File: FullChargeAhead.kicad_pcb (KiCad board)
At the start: 2 copper layers, 18 parts, among them P101 USB_OTG, P102 CONN_01X02, U101 MCP73834

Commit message: starting rev 2
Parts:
- removed D103: NOPOP, LEDs:LED_0805
- removed R106: NOPOP, Resistors_SMD:R_0805_HandSoldering
- added P103: JST_2PIN, FullChargeAhead:JST_Type_PH_Side_Entry_1x02_Pitch2.00mm, F.Cu at (164.2, 91.2)
- added R110: 10K, Resistors_SMD:R_0805_HandSoldering, F.Cu at (166.0, 102.7)
- P101: footprint Connect:USB_Micro-B_10103594-0001LF -> FullChargeAhead:USB_Micro-B_10103594-0001LF
- P102: footprint Connect:PINHEAD1-2 -> Pin_Headers:Pin_Header_Straight_1x02
- R107: value 38.3R -> 1K
- R108: value 0R -> 38.3R
- R109: value 10K -> 0R
- moved R103 82.8 mm to (129.8, 96.6), turned to 90 degrees
- moved D102 80.2 mm to (140.7, 103.5), turned to 180 degrees
- moved R102 75.4 mm to (132.5, 96.6), turned to 90 degrees
- moved D101 73.4 mm to (140.7, 101.0), turned to 180 degrees
- moved R101 68.6 mm to (135.1, 96.7), turned to 90 degrees
- moved P101 62.5 mm to (132.5, 89.2), turned to 180 degrees
- moved R105 62.3 mm to (145.9, 103.5)
- moved C101 60.8 mm to (141.9, 95.5)
- moved R104 59.2 mm to (145.9, 101.0)
- moved R109 57.0 mm to (160.4, 102.9), turned to 180 degrees
- moved R108 55.2 mm to (154.2, 105.8), turned to 180 degrees
- moved R107 51.2 mm to (160.0, 106.9)
- moved C102 44.8 mm to (164.1, 95.6), turned to 180 degrees
- moved U101 43.7 mm to (153.7, 102.2)
- moved P102 32.0 mm to (164.9, 107.6), turned to 90 degrees
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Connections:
- P102 pad 1: /Vbat -> Net-(P102-Pad1)
- R107 pad 2: GND -> Net-(P102-Pad1)
- R108 pad 2: Net-(R108-Pad2) -> GND
- R109 pad 1: GND -> Net-(R109-Pad1)
- R109 pad 2: Net-(R108-Pad1) -> Net-(R109-Pad2)
- TH101 pad 1: Net-(R108-Pad1) -> Net-(R109-Pad1)
- U101 pad 6: Net-(R107-Pad1) -> Net-(R108-Pad1)
- U101 pad 7: Net-(R106-Pad2) -> Net-(R107-Pad1)
- U101 pad 8: Net-(R108-Pad2) -> Net-(R109-Pad2)

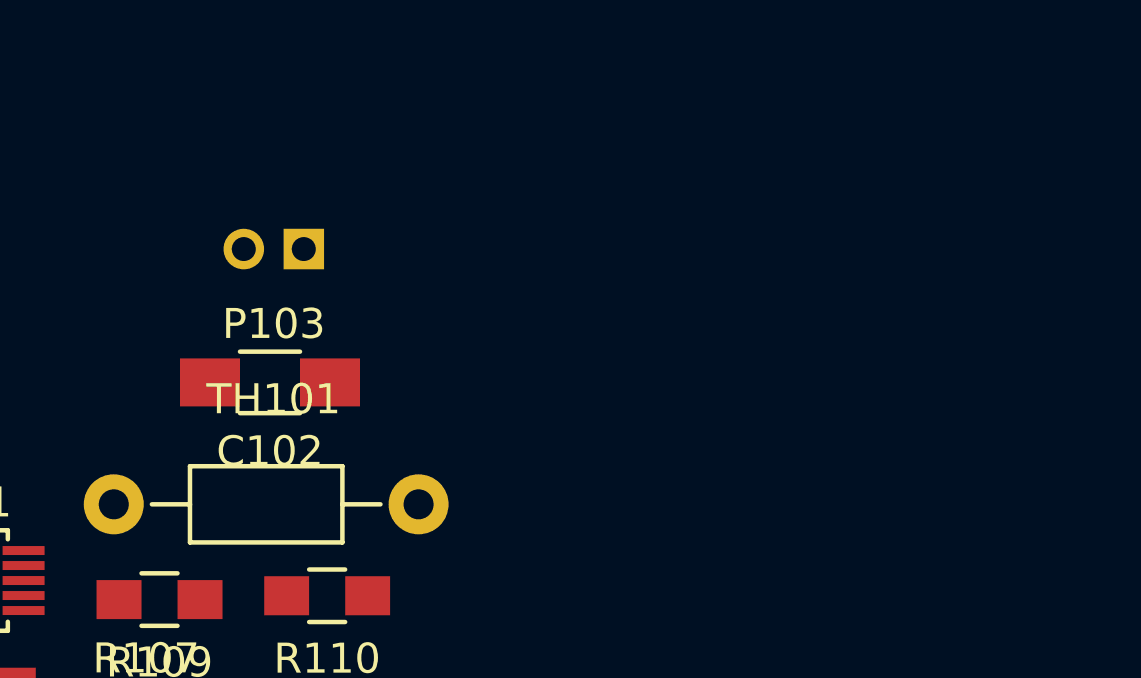
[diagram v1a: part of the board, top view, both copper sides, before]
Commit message: added Vbat connectors for current monitoring
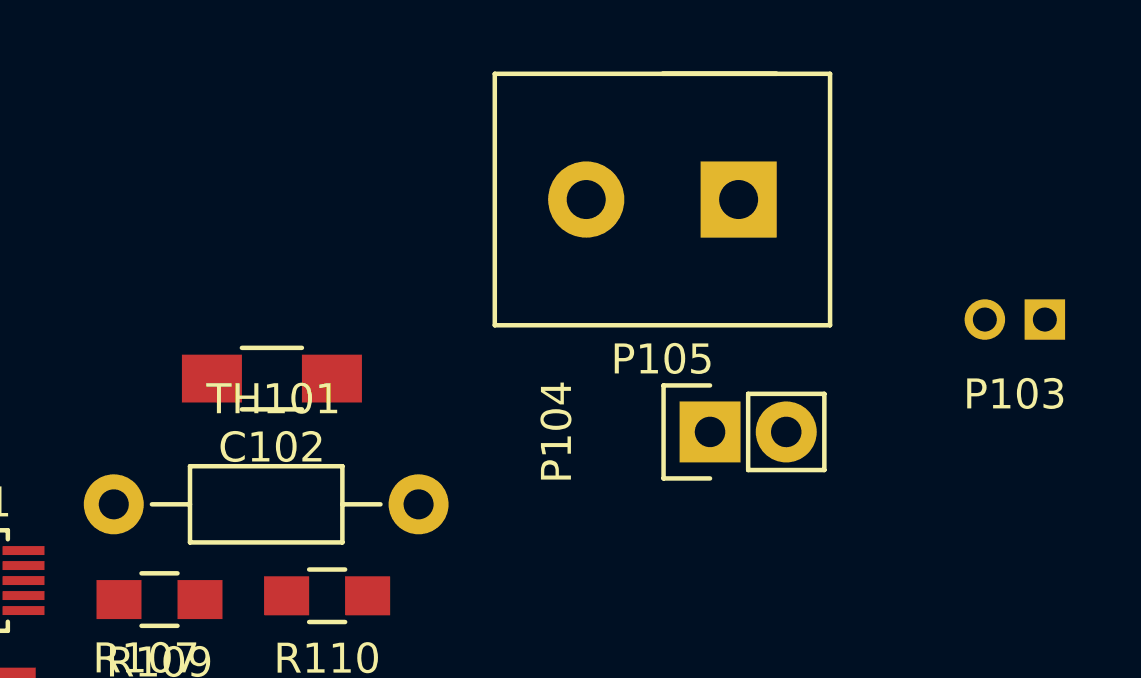
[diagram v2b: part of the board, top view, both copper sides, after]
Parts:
- added P104: CONN_01X02, Pin_Headers:Pin_Header_Straight_1x02, F.Cu at (178.8, 97.3)
- added P105: CONN_01X02, FullChargeAhead:Terminal_Block_200_mil, F.Cu at (177.2, 89.5)
- moved P103 24.8 mm to (188.9, 93.5)
- moved C102 0.14 mm to (164.1, 95.5)
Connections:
- P103 pad 1: /Vbat -> /Vbat2
- R110 pad 2: Net-(R109-Pad1) -> Net-(R110-Pad2)
- U101 pad 8: Net-(R109-Pad2) -> Net-(R110-Pad2)
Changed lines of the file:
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@@
 (kicad_pcb (version 4) (host pcbnew 4.0.2-stable)
   (general
-    (links 38)
-    (no_connects 38)
+    (links 40)
+    (no_connects 40)
     (area 0 0 0 0)
     (thickness 1.6)
@@
     (tracks 0)
     (zones 0)
-    (modules 18)
-    (nets 16)
+    (modules 20)
+    (nets 18)
   )
   (page A4)
@@
   (net 14 "Net-(R109-Pad2)")
   (net 15 "Net-(R107-Pad1)")
+  (net 16 /Vbat2)
+  (net 17 "Net-(R110-Pad2)")
   (net_class Default "This is the default net class."
     (clearance 0.2)
@@
     (uvia_drill 0.1)
     (add_net /Vbat)
+    (add_net /Vbat2)
     (add_net /Vdd)
     (add_net GND)
@@
     (add_net "Net-(R109-Pad1)")
     (add_net "Net-(R109-Pad2)")
+    (add_net "Net-(R110-Pad2)")
   )
   (module LEDs:LED_0805 (layer F.Cu)
@@
   )
   (module Capacitors_SMD:C_1206_HandSoldering (layer F.Cu)
-    (at 164.084 95.631 180)
+    (at 164.1475 95.504 180)
     (descr "Capacitor SMD 1206, hand soldering")
     (tags "capacitor 1206")
@@
       (net 15 "Net-(R107-Pad1)"))
     (pad 8 smd rect (at 2.2 0) (size 1.4 0.3) (layers F.Cu F.Paste F.Mask)
-      (net 14 "Net-(R109-Pad2)"))
+      (net 17 "Net-(R110-Pad2)"))
     (pad 9 smd rect (at 2.2 -0.5) (size 1.4 0.3) (layers F.Cu F.Paste F.Mask)
       (net 3 /Vbat))
@@
       (net 2 GND))
     (pad 2 smd rect (at 1.35 0 180) (size 1.5 1.3) (layers F.Cu F.Paste F.Mask)
-      (net 13 "Net-(R109-Pad1)"))
+      (net 17 "Net-(R110-Pad2)"))
     (model Resistors_SMD.3dshapes/R_0805_HandSoldering.wrl
       (at (xyz 0 0 0))
@@
   )
   (module FullChargeAhead:JST_Type_PH_Side_Entry_1x02_Pitch2.00mm (layer F.Cu)
-    (at 164.211 91.186)
+    (at 188.9125 93.5355)
     (descr "Through hole pin header, 1x02, 2.00mm pitch, single row")
     (tags "pin header single row")
@@
     (fp_line (start -2.95 -6.25) (end 2.95 -6.25) (layer F.CrtYd) (width 0.15))
     (pad 1 thru_hole rect (at 1 0 270) (size 1.35 1.35) (drill 0.8) (layers *.Cu *.Mask)
+      (net 16 /Vbat2))
+    (pad 2 thru_hole circle (at -1 0 270) (size 1.35 1.35) (drill 0.8) (layers *.Cu *.Mask)
+      (net 2 GND))
+    (model Pin_Headers.3dshapes/Pin_Header_Straight_1x02_Pitch2.00mm.wrl
+      (at (xyz 0 0 0))
+      (scale (xyz 1 1 1))
+      (rotate (xyz 0 0 0))
+    )
+  )
+  (module Pin_Headers:Pin_Header_Straight_1x02 (layer F.Cu)
+    (at 178.7525 97.282 90)
+    (descr "Through hole pin header")
+    (tags "pin header")
+    (fp_text reference P104 (at 0 -5.1 90) (layer F.SilkS)
+      (effects (font (size 1 1) (thickness 0.15)))
+    )
+    (fp_text value CONN_01X02 (at 0 -3.1 90) (layer F.Fab)
+      (effects (font (size 1 1) (thickness 0.15)))
+    )
+    (fp_line (start 1.27 1.27) (end 1.27 3.81) (layer F.SilkS) (width 0.15))
+    (fp_line (start 1.55 -1.55) (end 1.55 0) (layer F.SilkS) (width 0.15))
+    (fp_line (start -1.75 -1.75) (end -1.75 4.3) (layer F.CrtYd) (width 0.05))
+    (fp_line (start 1.75 -1.75) (end 1.75 4.3) (layer F.CrtYd) (width 0.05))
+    (fp_line (start -1.75 -1.75) (end 1.75 -1.75) (layer F.CrtYd) (width 0.05))
+    (fp_line (start -1.75 4.3) (end 1.75 4.3) (layer F.CrtYd) (width 0.05))
+    (fp_line (start 1.27 1.27) (end -1.27 1.27) (layer F.SilkS) (width 0.15))
+    (fp_line (start -1.55 0) (end -1.55 -1.55) (layer F.SilkS) (width 0.15))
+    (fp_line (start -1.55 -1.55) (end 1.55 -1.55) (layer F.SilkS) (width 0.15))
+    (fp_line (start -1.27 1.27) (end -1.27 3.81) (layer F.SilkS) (width 0.15))
+    (fp_line (start -1.27 3.81) (end 1.27 3.81) (layer F.SilkS) (width 0.15))
+    (pad 1 thru_hole rect (at 0 0 90) (size 2.032 2.032) (drill 1.016) (layers *.Cu *.Mask F.SilkS)
       (net 3 /Vbat))
-    (pad 2 thru_hole circle (at -1 0 270) (size 1.35 1.35) (drill 0.8) (layers *.Cu *.Mask)
-      (net 2 GND))
-    (model Pin_Headers.3dshapes/Pin_Header_Straight_1x02_Pitch2.00mm.wrl
-      (at (xyz 0 0 0))
-      (scale (xyz 1 1 1))
+    (pad 2 thru_hole oval (at 0 2.54 90) (size 2.032 2.032) (drill 1.016) (layers *.Cu *.Mask F.SilkS)
+      (net 16 /Vbat2))
+    (model Pin_Headers.3dshapes/Pin_Header_Straight_1x02.wrl
+      (at (xyz 0 -0.05 0))
+      (scale (xyz 1 1 1))
+      (rotate (xyz 0 0 90))
+    )
+  )
+  (module FullChargeAhead:Terminal_Block_200_mil (layer F.Cu)
+    (at 177.165 89.535 180)
+    (descr "Through hole pin header")
+    (tags "pin header")
+    (fp_text reference P105 (at 0 -5.334 180) (layer F.SilkS)
+      (effects (font (size 1 1) (thickness 0.15)))
+    )
+    (fp_text value CONN_01X02 (at 0.254 3.048 180) (layer F.SilkS) hide
+      (effects (font (size 1 1) (thickness 0.15)))
+    )
+    (fp_line (start -5.588 -4.191) (end -5.588 4.191) (layer F.SilkS) (width 0.15))
+    (fp_line (start -3.81 4.191) (end 0 4.191) (layer F.SilkS) (width 0.15))
+    (fp_line (start -5.588 4.191) (end 5.588 4.191) (layer F.SilkS) (width 0.15))
+    (fp_line (start 5.588 4.191) (end 5.588 -4.191) (layer F.SilkS) (width 0.15))
+    (fp_line (start 5.588 -4.191) (end -5.588 -4.191) (layer F.SilkS) (width 0.15))
+    (pad 1 thru_hole rect (at -2.54 0 180) (size 2.54 2.54) (drill 1.30048) (layers *.Cu *.Mask F.SilkS)
+      (net 16 /Vbat2))
+    (pad 2 thru_hole oval (at 2.54 0 180) (size 2.54 2.54) (drill 1.30048) (layers *.Cu *.Mask F.SilkS)
+      (net 3 /Vbat))
+    (model Pin_Headers/Pin_Header_Straight_1x02.wrl
+      (at (xyz 0 0 0))
+      (scale (xyz 1 1 1))

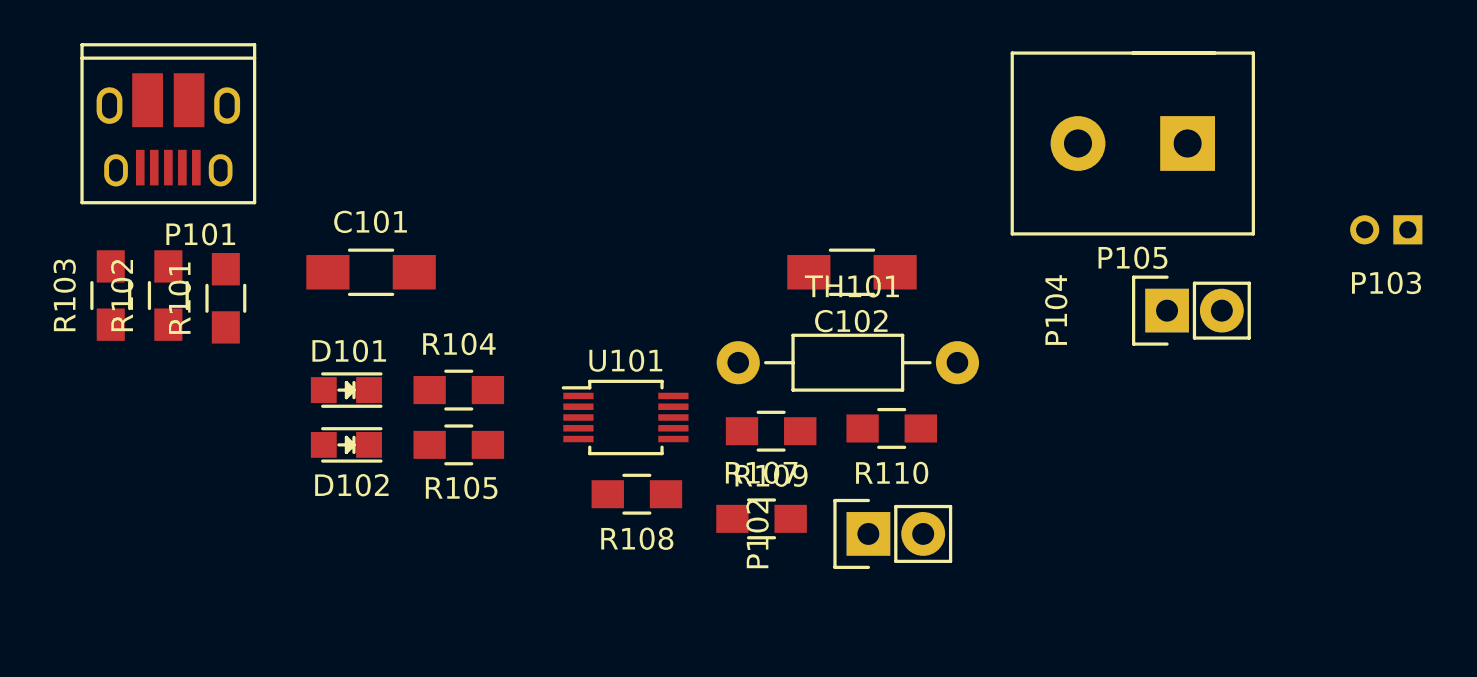
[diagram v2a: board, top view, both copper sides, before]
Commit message: initial board layout and copper fills
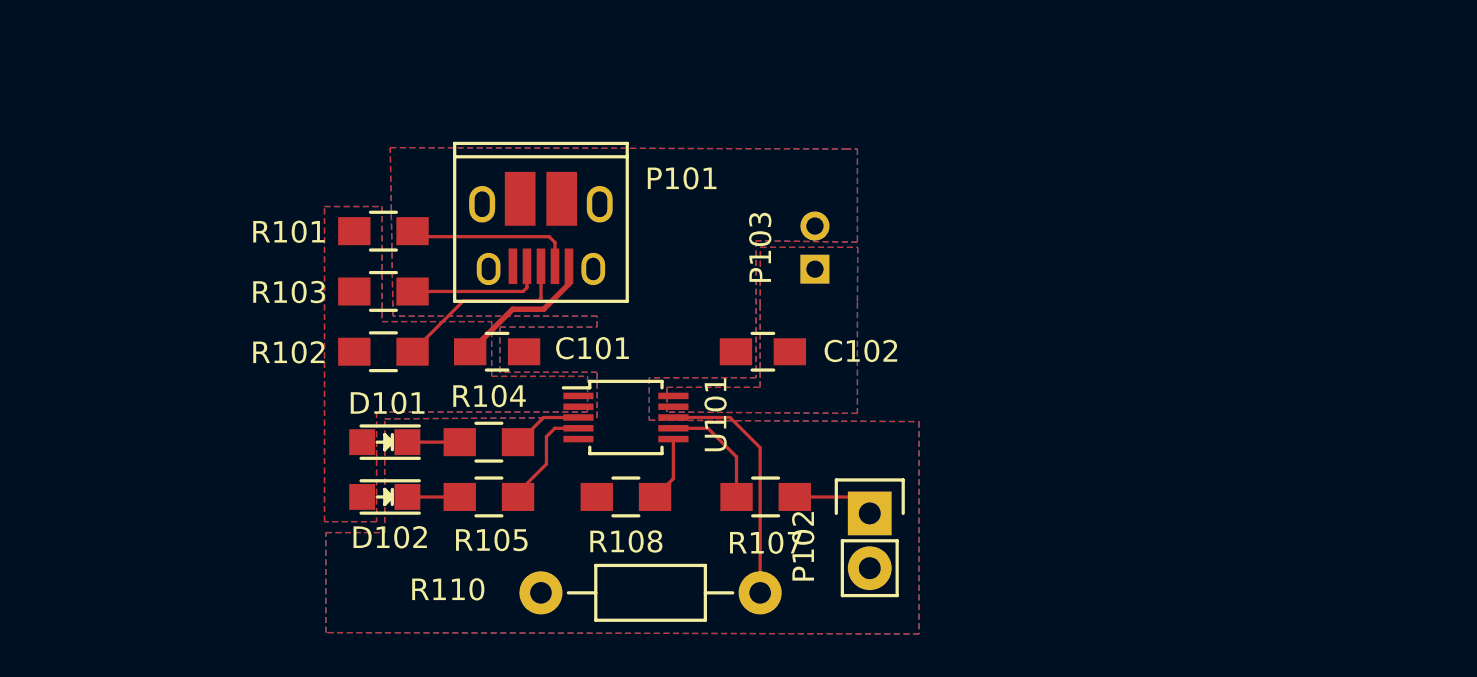
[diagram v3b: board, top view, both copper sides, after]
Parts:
- removed P104: CONN_01X02, Pin_Headers:Pin_Header_Straight_1x02
- removed P105: CONN_01X02, FullChargeAhead:Terminal_Block_200_mil
- removed R109: 0R, Resistors_SMD:R_0805_HandSoldering
- removed TH101: THERMISTOR, Resistors_ThroughHole:Resistor_Horizontal_RM10mm
- C101, C102: footprint Capacitors_SMD:C_1206_HandSoldering -> Capacitors_SMD:C_0805_HandSoldering
- D101: value LED -> YELLOW
- D102: value LED -> GREEN
- R104, R105: value 470 -> 430
- R108: value 38.3R -> 8.2K
- R110: footprint Resistors_SMD:R_0805_HandSoldering -> Resistors_ThroughHole:Resistor_Horizontal_RM10mm
- moved P103 26.5 mm to (162.4, 94.4), turned to 270 degrees
- moved R110 18.0 mm to (149.7, 110.4), turned to 0 degrees
- moved P101 17.9 mm to (149.7, 93.7)
- moved R103 12.6 mm to (142.4, 96.4), turned to 0 degrees
- moved R102 10.3 mm to (142.4, 99.2), turned to 0 degrees
- moved R101 7.94 mm to (142.4, 93.6), turned to 0 degrees
- moved C101 6.91 mm to (147.7, 99.2)
- moved C102 5.53 mm to (160.0, 99.2)
- moved D102 3.00 mm to (142.5, 105.9)
- moved D101 3.00 mm to (142.5, 103.4)
- moved R105 2.79 mm to (147.3, 105.9)
- moved R104 2.79 mm to (147.3, 103.4)
- moved R107 1.03 mm to (160.1, 105.9)
- moved P102 0.95 mm to (165.0, 106.7), turned to 0 degrees
- moved R108 0.52 mm to (153.7, 105.9)
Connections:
- P103 pad 1: /Vbat2 -> /Vbat
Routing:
- net Net-(R110-Pad2): track 0.00 -> 11.3 mm
- net Net-(P101-Pad3): track 0.00 -> 8.46 mm
- net Net-(P101-Pad2): track 0.00 -> 7.92 mm
- net /Vdd: track 0.00 -> 6.70 mm
- net Net-(P101-Pad4): track 0.00 -> 6.37 mm
- net Net-(R107-Pad1): track 0.00 -> 5.33 mm
- net Net-(R105-Pad2): track 0.00 -> 4.98 mm
- net Net-(P102-Pad1): track 0.00 -> 3.79 mm
- net Net-(R104-Pad2): track 0.00 -> 3.27 mm
- net Net-(R108-Pad1): track 0.00 -> 3.04 mm
- net Net-(D102-Pad1): track 0.00 -> 2.43 mm
- net Net-(D101-Pad1): track 0.00 -> 2.43 mm
- added copper zone on B.Cu, net /Vbat
- added copper zone on F.Cu, net /Vbat
- added copper zone on B.Cu, net /Vdd
- added copper zone on F.Cu, net /Vdd
- added copper zone on B.Cu, net GND
- added copper zone on F.Cu, net GND
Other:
- net class Default: clearance 0.2 -> 0.1524; trace_width 0.25 -> 0.1524; via_dia 0.6 -> 0.6858; via_drill 0.4 -> 0.3302
- rule trace_clearance: 0.2 -> 0.1524
- rule trace_min: 0.2 -> 0.1524
- rule via_min_drill: 0.3 -> 0.3302
- rule via_min_size: 0.4 -> 0.6858
